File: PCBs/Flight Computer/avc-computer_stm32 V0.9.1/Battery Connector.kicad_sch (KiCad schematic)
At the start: 3 parts, among them J2 Conn_01x02_Female, J4 ESC Power

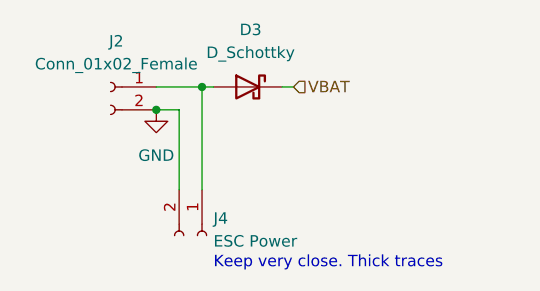
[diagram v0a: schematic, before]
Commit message: Fixed all issues except for 5v buck inductor heating
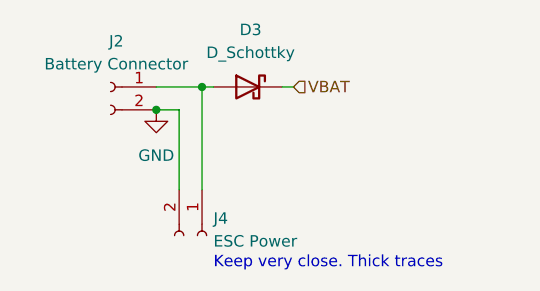
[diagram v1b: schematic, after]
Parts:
- J2: value Conn_01x02_Female -> Battery Connector
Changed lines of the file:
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@@
-(kicad_sch (version 20211123) (generator eeschema)
+(kicad_sch (version 20230121) (generator eeschema)
   (paper "A4")
   (junction (at 143.51 82.55) (diameter 0) (color 0 0 0 0)
@@
   )
   (wire (pts (xy 148.59 80.01) (xy 148.59 91.44))
-    (stroke (width 0) (type default) (color 0 0 0 0))
+    (stroke (width 0) (type default))
   )
   (wire (pts (xy 143.51 80.01) (xy 148.59 80.01))
-    (stroke (width 0) (type default) (color 0 0 0 0))
+    (stroke (width 0) (type default))
   )
   (wire (pts (xy 146.05 91.44) (xy 146.05 82.55))
-    (stroke (width 0) (type default) (color 0 0 0 0))
+    (stroke (width 0) (type default))
   )
   (wire (pts (xy 146.05 82.55) (xy 143.51 82.55))
-    (stroke (width 0) (type default) (color 0 0 0 0))
+    (stroke (width 0) (type default))
   )
   (wire (pts (xy 157.48 80.01) (xy 158.75 80.01))
-    (stroke (width 0) (type default) (color 0 0 0 0))
+    (stroke (width 0) (type default))
   )
   (wire (pts (xy 149.86 80.01) (xy 148.59 80.01))
-    (stroke (width 0) (type default) (color 0 0 0 0))
+    (stroke (width 0) (type default))
   )
   (text "Keep very close. Thick traces" (at 149.86 100.33 0)
     (effects (font (size 1.27 1.27)) (justify left bottom))
   )
-  (hierarchical_label "VBAT" (shape input) (at 158.75 80.01 0)
+  (hierarchical_label "VBAT" (shape input) (at 158.75 80.01 0) (fields_autoplaced)
     (effects (font (size 1.27 1.27)) (justify left))
   )
   (symbol (lib_id "power:GND") (at 143.51 82.55 0) (unit 1)
-    (in_bom yes) (on_board yes) (fields_autoplaced)
-    (property "Reference" "#PWR0150" (id 0) (at 143.51 88.9 0)
+    (in_bom yes) (on_board yes) (dnp no) (fields_autoplaced)
+    (property "Reference" "#PWR0150" (at 143.51 88.9 0)
       (effects (font (size 1.27 1.27)) hide)
     )
-    (property "Value" "GND" (id 1) (at 143.51 87.63 0))
-    (property "Footprint" "" (id 2) (at 143.51 82.55 0)
+    (property "Value" "GND" (at 143.51 87.63 0)
+      (effects (font (size 1.27 1.27)))
+    )
+    (property "Footprint" "" (at 143.51 82.55 0)
       (effects (font (size 1.27 1.27)) hide)
     )
-    (property "Datasheet" "" (id 3) (at 143.51 82.55 0)
+    (property "Datasheet" "" (at 143.51 82.55 0)
       (effects (font (size 1.27 1.27)) hide)
     )
     (pin "1")
+    (instances
+      (project "avc-computer"
+        (path "/e63e39d7-6ac0-4ffd-8aa3-1841a4541b55/feb67fac-24a5-46c8-b058-e8d08103a624"
+          (reference "#PWR0150") (unit 1)
+        )
+      )
+    )
   )
   (symbol (lib_id "Device:D_Schottky") (at 153.67 80.01 0) (mirror y) (unit 1)
-    (in_bom yes) (on_board yes) (fields_autoplaced)
-    (property "Reference" "D3" (id 0) (at 153.9875 73.66 0))
-    (property "Value" "D_Schottky" (id 1) (at 153.9875 76.2 0))
-    (property "Footprint" "B320A-13-F:DIOM5226X230N" (id 2) (at 153.67 80.01 0)
+    (in_bom yes) (on_board yes) (dnp no) (fields_autoplaced)
+    (property "Reference" "D3" (at 153.9875 73.66 0)
+      (effects (font (size 1.27 1.27)))
+    )
+    (property "Value" "D_Schottky" (at 153.9875 76.2 0)
+      (effects (font (size 1.27 1.27)))
+    )
+    (property "Footprint" "B320A-13-F:DIOM5226X230N" (at 153.67 80.01 0)
       (effects (font (size 1.27 1.27)) hide)
     )
-    (property "Datasheet" "~" (id 3) (at 153.67 80.01 0)
+    (property "Datasheet" "~" (at 153.67 80.01 0)
       (effects (font (size 1.27 1.27)) hide)
     )
     (pin "1")
     (pin "2")
+    (instances
+      (project "avc-computer"
+        (path "/e63e39d7-6ac0-4ffd-8aa3-1841a4541b55/feb67fac-24a5-46c8-b058-e8d08103a624"
+          (reference "D3") (unit 1)
+        )
+      )
+    )
   )
   (symbol (lib_id "Connector:Conn_01x02_Female") (at 138.43 80.01 0) (mirror y) (unit 1)
-    (in_bom yes) (on_board yes) (fields_autoplaced)
-    (property "Reference" "J2" (id 0) (at 139.065 74.93 0))
-    (property "Value" "Conn_01x02_Female" (id 1) (at 139.065 77.47 0))
-    (property "Footprint" "Connector_Wire:SolderWire-2sqmm_1x02_P7.8mm_D2mm_OD3.9mm" (id 2) (at 138.43 80.01 0)
+    (in_bom yes) (on_board yes) (dnp no) (fields_autoplaced)
+    (property "Reference" "J2" (at 139.065 74.93 0)
+      (effects (font (size 1.27 1.27)))
+    )
+    (property "Value" "Battery Connector" (at 139.065 77.47 0)
+      (effects (font (size 1.27 1.27)))
+    )
+    (property "Footprint" "Connector_Wire:SolderWire-2sqmm_1x02_P7.8mm_D2mm_OD3.9mm" (at 138.43 80.01 0)
       (effects (font (size 1.27 1.27)) hide)
     )
-    (property "Datasheet" "~" (id 3) (at 138.43 80.01 0)
+    (property "Datasheet" "~" (at 138.43 80.01 0)
       (effects (font (size 1.27 1.27)) hide)
     )
     (pin "1")
     (pin "2")
+    (instances
+      (project "avc-computer"
+        (path "/e63e39d7-6ac0-4ffd-8aa3-1841a4541b55/feb67fac-24a5-46c8-b058-e8d08103a624"
+          (reference "J2") (unit 1)
+        )
+      )
+    )
   )
   (symbol (lib_id "Connector:Conn_01x02_Female") (at 148.59 96.52 270) (unit 1)
-    (in_bom yes) (on_board yes) (fields_autoplaced)
-    (property "Reference" "J4" (id 0) (at 149.86 94.6149 90)
+    (in_bom yes) (on_board yes) (dnp no) (fields_autoplaced)
+    (property "Reference" "J4" (at 149.86 94.6149 90)
       (effects (font (size 1.27 1.27)) (justify left))
     )
-    (property "Value" "ESC Power" (id 1) (at 149.86 97.1549 90)
+    (property "Value" "ESC Power" (at 149.86 97.1549 90)
       (effects (font (size 1.27 1.27)) (justify left))
     )
-    (property "Footprint" "Connector_Wire:SolderWire-2sqmm_1x02_P7.8mm_D2mm_OD3.9mm" (id 2) (at 148.59 96.52 0)
+    (property "Footprint" "Connector_Wire:SolderWire-2sqmm_1x02_P7.8mm_D2mm_OD3.9mm" (at 148.59 96.52 0)
       (effects (font (size 1.27 1.27)) hide)
     )
-    (property "Datasheet" "~" (id 3) (at 148.59 96.52 0)
+    (property "Datasheet" "~" (at 148.59 96.52 0)
       (effects (font (size 1.27 1.27)) hide)
     )
     (pin "1")
     (pin "2")
+    (instances
+      (project "avc-computer"
+        (path "/e63e39d7-6ac0-4ffd-8aa3-1841a4541b55/feb67fac-24a5-46c8-b058-e8d08103a624"
+          (reference "J4") (unit 1)
+        )
+      )
+    )
   )
 )
